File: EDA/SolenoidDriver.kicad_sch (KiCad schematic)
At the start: 16 parts, among them U9 LMR62014XMF

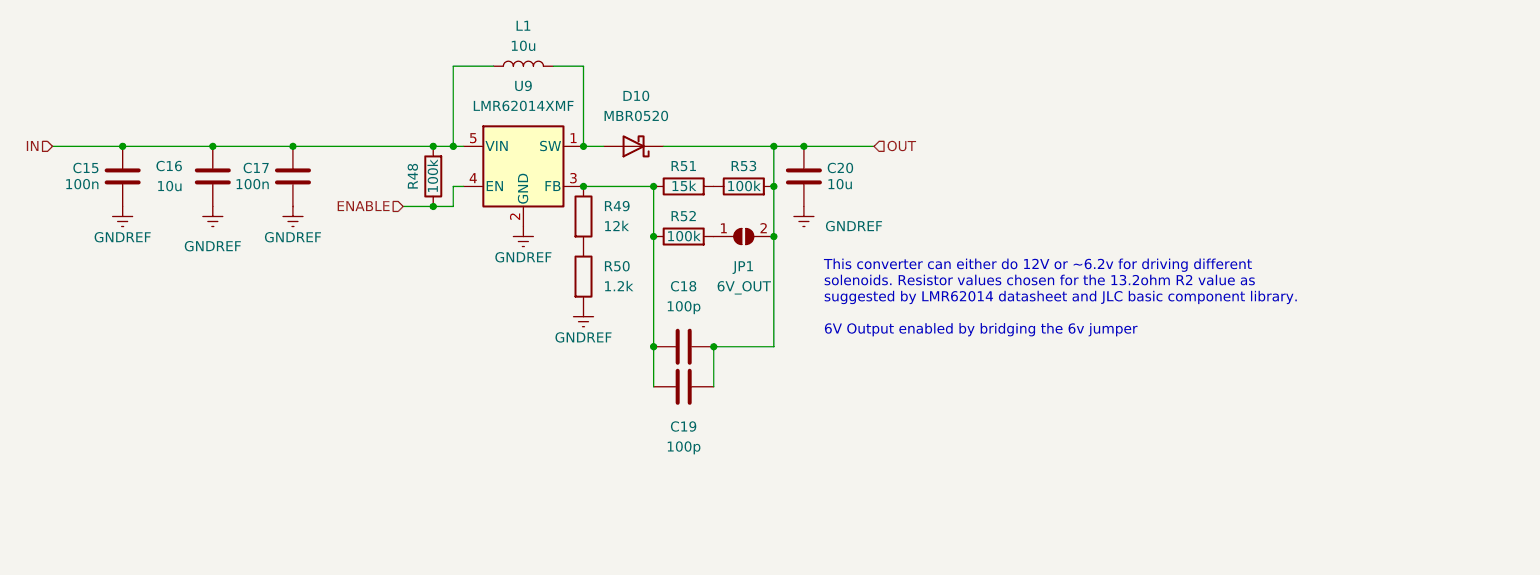
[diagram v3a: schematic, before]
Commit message: Move power logic into power distribution sheet
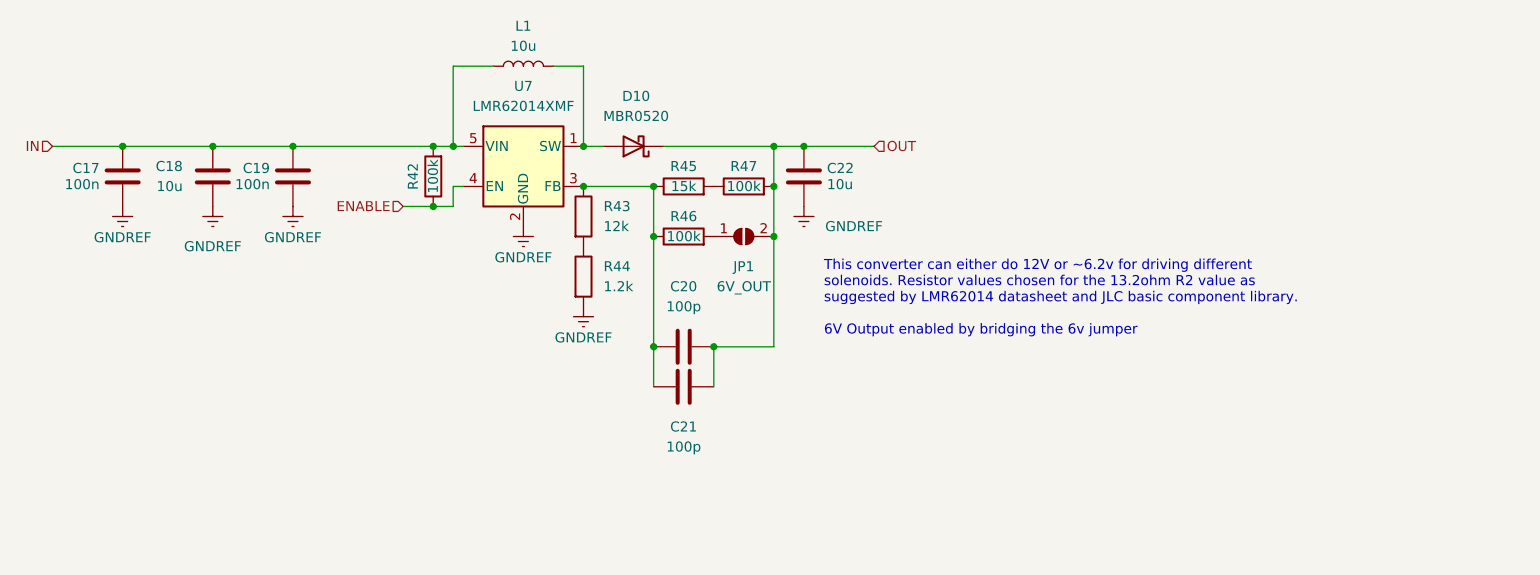
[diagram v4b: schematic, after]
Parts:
- renumbered C15 to C17, C16 to C18, C17 to C19, C18 to C20, C19 to C21, C20 to C22, R48 to R42, R49 to R43, R50 to R44, R51 to R45, R52 to R46, R53 to R47, U9 to U7
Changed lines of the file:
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@@
   (symbol (lib_id "power:GNDREF") (at 92.71 74.93 0) (unit 1)
     (in_bom yes) (on_board yes) (dnp no) (fields_autoplaced)
-    (property "Reference" "#PWR060" (at 92.71 81.28 0)
+    (property "Reference" "#PWR056" (at 92.71 81.28 0)
       (effects (font (size 1.27 1.27)) hide)
     )
@@
       (project "DiveCAN Head2"
         (path "/ab021047-3849-453b-b3dc-d234ace3779d/9021e904-ec93-4c28-9903-7bba14359351"
-          (reference "#PWR060") (unit 1)
+          (reference "#PWR056") (unit 1)
         )
       )
@@
   (symbol (lib_id "Library:R") (at 163.83 72.39 90) (unit 1)
     (in_bom yes) (on_board yes) (dnp no)
-    (property "Reference" "R51" (at 163.83 69.85 90)
+    (property "Reference" "R45" (at 163.83 69.85 90)
       (effects (font (size 1.27 1.27)))
     )
@@
       (project "DiveCAN Head2"
         (path "/ab021047-3849-453b-b3dc-d234ace3779d/9021e904-ec93-4c28-9903-7bba14359351"
-          (reference "R51") (unit 1)
+          (reference "R45") (unit 1)
         )
       )
@@
   (symbol (lib_id "Library:R") (at 151.13 76.2 0) (unit 1)
     (in_bom yes) (on_board yes) (dnp no) (fields_autoplaced)
-    (property "Reference" "R49" (at 153.67 74.93 0)
+    (property "Reference" "R43" (at 153.67 74.93 0)
       (effects (font (size 1.27 1.27)) (justify left))
     )
@@
       (project "DiveCAN Head2"
         (path "/ab021047-3849-453b-b3dc-d234ace3779d/9021e904-ec93-4c28-9903-7bba14359351"
-          (reference "R49") (unit 1)
+          (reference "R43") (unit 1)
         )
       )
@@
   (symbol (lib_id "Library:R") (at 132.08 71.12 180) (unit 1)
     (in_bom yes) (on_board yes) (dnp no)
-    (property "Reference" "R48" (at 129.54 71.12 90)
+    (property "Reference" "R42" (at 129.54 71.12 90)
       (effects (font (size 1.27 1.27)))
     )
@@
       (project "DiveCAN Head2"
         (path "/ab021047-3849-453b-b3dc-d234ace3779d/9021e904-ec93-4c28-9903-7bba14359351"
-          (reference "R48") (unit 1)
+          (reference "R42") (unit 1)
         )
       )
@@
   (symbol (lib_id "power:GNDREF") (at 151.13 87.63 0) (unit 1)
     (in_bom yes) (on_board yes) (dnp no) (fields_autoplaced)
-    (property "Reference" "#PWR064" (at 151.13 93.98 0)
+    (property "Reference" "#PWR060" (at 151.13 93.98 0)
       (effects (font (size 1.27 1.27)) hide)
     )
@@
       (project "DiveCAN Head2"
         (path "/ab021047-3849-453b-b3dc-d234ace3779d/9021e904-ec93-4c28-9903-7bba14359351"
-          (reference "#PWR064") (unit 1)
+          (reference "#PWR060") (unit 1)
         )
       )
@@
   (symbol (lib_id "Regulator_Switching:LMR62014XMF") (at 143.51 69.85 0) (unit 1)
     (in_bom yes) (on_board yes) (dnp no) (fields_autoplaced)
-    (property "Reference" "U9" (at 143.51 59.69 0)
+    (property "Reference" "U7" (at 143.51 59.69 0)
       (effects (font (size 1.27 1.27)))
     )
@@
       (project "DiveCAN Head2"
         (path "/ab021047-3849-453b-b3dc-d234ace3779d/9021e904-ec93-4c28-9903-7bba14359351"
-          (reference "U9") (unit 1)
+          (reference "U7") (unit 1)
         )
       )
@@
   (symbol (lib_id "Library:C") (at 114.3 71.12 180) (unit 1)
     (in_bom yes) (on_board yes) (dnp no) (fields_autoplaced)
-    (property "Reference" "C17" (at 111.3791 70.096 0)
+    (property "Reference" "C19" (at 111.3791 70.096 0)
       (effects (font (size 1.27 1.27)) (justify left))
     )
@@
       (project "DiveCAN Head2"
         (path "/ab021047-3849-453b-b3dc-d234ace3779d/9021e904-ec93-4c28-9903-7bba14359351"
-          (reference "C17") (unit 1)
+          (reference "C19") (unit 1)
         )
       )
@@
   (symbol (lib_id "power:GNDREF") (at 114.3 74.93 0) (unit 1)
     (in_bom yes) (on_board yes) (dnp no) (fields_autoplaced)
-    (property "Reference" "#PWR062" (at 114.3 81.28 0)
+    (property "Reference" "#PWR058" (at 114.3 81.28 0)
       (effects (font (size 1.27 1.27)) hide)
     )
@@
       (project "DiveCAN Head2"
         (path "/ab021047-3849-453b-b3dc-d234ace3779d/9021e904-ec93-4c28-9903-7bba14359351"
-          (reference "#PWR062") (unit 1)
+          (reference "#PWR058") (unit 1)
         )
       )
@@
   (symbol (lib_id "Library:R") (at 163.83 78.74 90) (unit 1)
     (in_bom yes) (on_board yes) (dnp no)
-    (property "Reference" "R52" (at 163.83 76.2 90)
+    (property "Reference" "R46" (at 163.83 76.2 90)
       (effects (font (size 1.27 1.27)))
     )
@@
       (project "DiveCAN Head2"
         (path "/ab021047-3849-453b-b3dc-d234ace3779d/9021e904-ec93-4c28-9903-7bba14359351"
-          (reference "R52") (unit 1)
+          (reference "R46") (unit 1)
         )
       )
@@
   (symbol (lib_id "Library:C") (at 104.14 71.12 0) (unit 1)
     (in_bom yes) (on_board yes) (dnp no) (fields_autoplaced)
-    (property "Reference" "C16" (at 100.33 69.85 0)
+    (property "Reference" "C18" (at 100.33 69.85 0)
       (effects (font (size 1.27 1.27)) (justify right))
     )
@@
       (project "DiveCAN Head2"
         (path "/ab021047-3849-453b-b3dc-d234ace3779d/9021e904-ec93-4c28-9903-7bba14359351"
-          (reference "C16") (unit 1)
+          (reference "C18") (unit 1)
         )
       )
@@
   (symbol (lib_id "power:GNDREF") (at 179.07 74.93 0) (unit 1)
     (in_bom yes) (on_board yes) (dnp no)
-    (property "Reference" "#PWR065" (at 179.07 81.28 0)
+    (property "Reference" "#PWR061" (at 179.07 81.28 0)
       (effects (font (size 1.27 1.27)) hide)
     )
@@
       (project "DiveCAN Head2"
         (path "/ab021047-3849-453b-b3dc-d234ace3779d/9021e904-ec93-4c28-9903-7bba14359351"
-          (reference "#PWR065") (unit 1)
+          (reference "#PWR061") (unit 1)
         )
       )
@@
   (symbol (lib_id "Library:C") (at 163.83 97.79 270) (unit 1)
     (in_bom yes) (on_board yes) (dnp no) (fields_autoplaced)
-    (property "Reference" "C19" (at 163.83 102.87 90)
+    (property "Reference" "C21" (at 163.83 102.87 90)
       (effects (font (size 1.27 1.27)))
     )
@@
       (project "DiveCAN Head2"
         (path "/ab021047-3849-453b-b3dc-d234ace3779d/9021e904-ec93-4c28-9903-7bba14359351"
-          (reference "C19") (unit 1)
+          (reference "C21") (unit 1)
         )
       )
@@
   (symbol (lib_id "Library:C") (at 163.83 92.71 270) (unit 1)
     (in_bom yes) (on_board yes) (dnp no) (fields_autoplaced)
-    (property "Reference" "C18" (at 163.83 85.09 90)
+    (property "Reference" "C20" (at 163.83 85.09 90)
       (effects (font (size 1.27 1.27)))
     )
@@
       (project "DiveCAN Head2"
         (path "/ab021047-3849-453b-b3dc-d234ace3779d/9021e904-ec93-4c28-9903-7bba14359351"
-          (reference "C18") (unit 1)
+          (reference "C20") (unit 1)
         )
       )
@@
   (symbol (lib_id "power:GNDREF") (at 143.51 77.47 0) (unit 1)
     (in_bom yes) (on_board yes) (dnp no) (fields_autoplaced)
-    (property "Reference" "#PWR063" (at 143.51 83.82 0)
+    (property "Reference" "#PWR059" (at 143.51 83.82 0)
       (effects (font (size 1.27 1.27)) hide)
     )
@@
       (project "DiveCAN Head2"
         (path "/ab021047-3849-453b-b3dc-d234ace3779d/9021e904-ec93-4c28-9903-7bba14359351"
-          (reference "#PWR063") (unit 1)
+          (reference "#PWR059") (unit 1)
         )
       )
@@
   (symbol (lib_id "Library:R") (at 151.13 83.82 0) (unit 1)
     (in_bom yes) (on_board yes) (dnp no) (fields_autoplaced)
-    (property "Reference" "R50" (at 153.67 82.55 0)
+    (property "Reference" "R44" (at 153.67 82.55 0)
       (effects (font (size 1.27 1.27)) (justify left))
     )
@@
       (project "DiveCAN Head2"
         (path "/ab021047-3849-453b-b3dc-d234ace3779d/9021e904-ec93-4c28-9903-7bba14359351"
-          (reference "R50") (unit 1)
+          (reference "R44") (unit 1)
         )
       )
@@
   (symbol (lib_id "Library:R") (at 171.45 72.39 90) (unit 1)
     (in_bom yes) (on_board yes) (dnp no)
-    (property "Reference" "R53" (at 171.45 69.85 90)
+    (property "Reference" "R47" (at 171.45 69.85 90)
       (effects (font (size 1.27 1.27)))
     )
@@
       (project "DiveCAN Head2"
         (path "/ab021047-3849-453b-b3dc-d234ace3779d/9021e904-ec93-4c28-9903-7bba14359351"
-          (reference "R53") (unit 1)
+          (reference "R47") (unit 1)
         )
       )
@@
   (symbol (lib_id "Library:C") (at 179.07 71.12 0) (unit 1)
     (in_bom yes) (on_board yes) (dnp no) (fields_autoplaced)
-    (property "Reference" "C20" (at 181.991 70.096 0)
+    (property "Reference" "C22" (at 181.991 70.096 0)
       (effects (font (size 1.27 1.27)) (justify left))
     )
@@
       (project "DiveCAN Head2"
         (path "/ab021047-3849-453b-b3dc-d234ace3779d/9021e904-ec93-4c28-9903-7bba14359351"
-          (reference "C20") (unit 1)
+          (reference "C22") (unit 1)
         )
       )
@@
   (symbol (lib_id "power:GNDREF") (at 104.14 74.93 0) (unit 1)
     (in_bom yes) (on_board yes) (dnp no) (fields_autoplaced)
-    (property "Reference" "#PWR061" (at 104.14 81.28 0)
+    (property "Reference" "#PWR057" (at 104.14 81.28 0)
       (effects (font (size 1.27 1.27)) hide)
     )
@@
       (project "DiveCAN Head2"
         (path "/ab021047-3849-453b-b3dc-d234ace3779d/9021e904-ec93-4c28-9903-7bba14359351"
-          (reference "#PWR061") (unit 1)
+          (reference "#PWR057") (unit 1)
         )
       )
@@
   (symbol (lib_id "Library:C") (at 92.71 71.12 180) (unit 1)
     (in_bom yes) (on_board yes) (dnp no) (fields_autoplaced)
-    (property "Reference" "C15" (at 89.7891 70.096 0)
+    (property "Reference" "C17" (at 89.7891 70.096 0)
       (effects (font (size 1.27 1.27)) (justify left))
     )
@@
       (project "DiveCAN Head2"
         (path "/ab021047-3849-453b-b3dc-d234ace3779d/9021e904-ec93-4c28-9903-7bba14359351"
-          (reference "C15") (unit 1)
-        )
-      )
+          (reference "C17") (unit 1)
+        )
+      )

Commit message: Add input protection to the power distribution
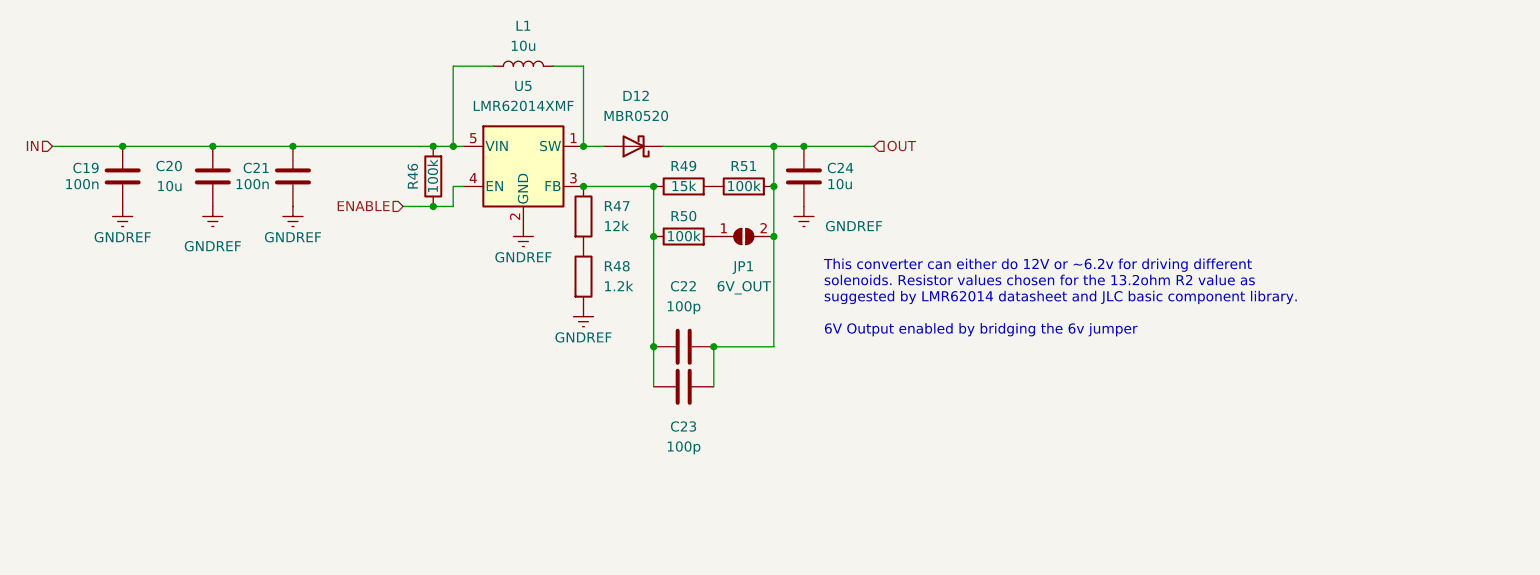
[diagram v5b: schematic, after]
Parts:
- JP1: footprint (none) -> Jumper:SolderJumper-2_P1.3mm_Open_TrianglePad1.0x1.5mm
- renumbered C17 to C19, C18 to C20, C19 to C21, C20 to C22, C21 to C23, C22 to C24, D10 to D12, R42 to R46, R43 to R47, R44 to R48, R45 to R49, R46 to R50, R47 to R51, U7 to U5

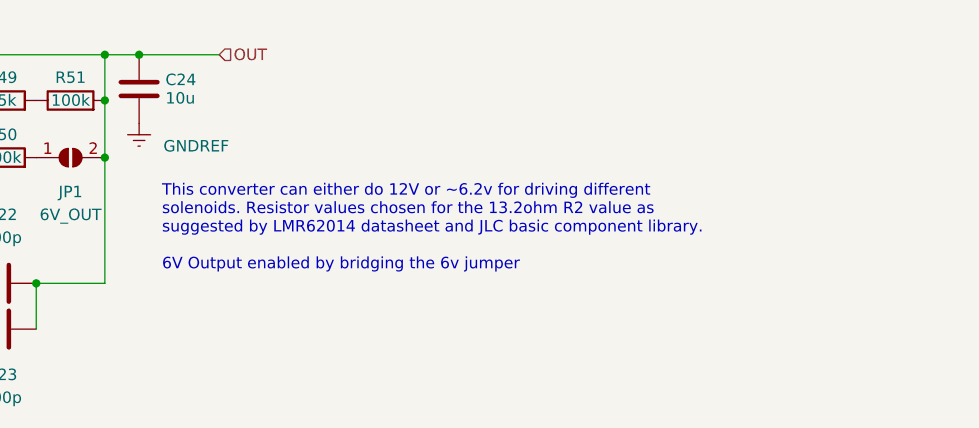
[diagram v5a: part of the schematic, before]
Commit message: Change solenoid power switch to TPS2121
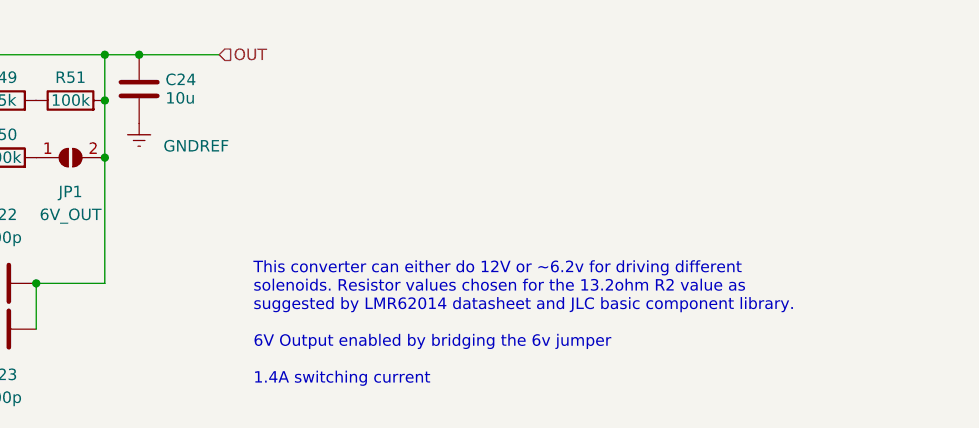
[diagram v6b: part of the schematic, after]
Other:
- note added: "This converter can either do 12V or ~6.2v for driving different solenoids. Resistor values chosen for the 13.2ohm R2 value as suggested by LMR62014 datasheet and JLC basic component library. 6V Output enabled by bridging the 6v jumper 1.4A switching current"
- note removed: "This converter can either do 12V or ~6.2v for driving different solenoids. Resistor values chosen for the 13.2ohm R2 value as suggested by LMR62014 datasheet and JLC basic component library. 6V Output enabled by bridging the 6v jumper"
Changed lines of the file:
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@@
     (stroke (width 0) (type default))
   )
-  (text "This converter can either do 12V or ~6.2v for driving different\nsolenoids. Resistor values chosen for the 13.2ohm R2 value as \nsuggested by LMR62014 datasheet and JLC basic component library.\n\n6V Output enabled by bridging the 6v jumper"
-    (at 181.61 91.44 0)
+  (text "This converter can either do 12V or ~6.2v for driving different\nsolenoids. Resistor values chosen for the 13.2ohm R2 value as \nsuggested by LMR62014 datasheet and JLC basic component library.\n\n6V Output enabled by bridging the 6v jumper\n\n1.4A switching current"
+    (at 191.77 104.14 0)
     (effects (font (size 1.27 1.27)) (justify left bottom))
   )

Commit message: Draft Rev2 PCB
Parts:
- L1: footprint (none) -> Library:L_SunItech_SLO0530H; MPN C879423 -> C325966
- U5: MPN (none) -> C468235
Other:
- note added: "This converter can either do 12V or ~6.2v for driving different solenoids. Resistor values chosen for the 13.2kohm R2 value as suggested by LMR62014 datasheet and JLC basic component library. 6V Output enabled by bridging the 6v jumper 1.4A switching current"
- note removed: "This converter can either do 12V or ~6.2v for driving different solenoids. Resistor values chosen for the 13.2ohm R2 value as suggested by LMR62014 datasheet and JLC basic component library. 6V Output enabled by bridging the 6v jumper 1.4A switching current"
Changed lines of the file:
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@@
     (stroke (width 0) (type default))
   )
-  (text "This converter can either do 12V or ~6.2v for driving different\nsolenoids. Resistor values chosen for the 13.2ohm R2 value as \nsuggested by LMR62014 datasheet and JLC basic component library.\n\n6V Output enabled by bridging the 6v jumper\n\n1.4A switching current"
-    (at 191.77 104.14 0)
+  (text "This converter can either do 12V or ~6.2v for driving different\nsolenoids. Resistor values chosen for the 13.2kohm R2 value as \nsuggested by LMR62014 datasheet and JLC basic component library.\n\n6V Output enabled by bridging the 6v jumper\n\n1.4A switching current"
+    (at 184.15 95.25 0)
     (effects (font (size 1.27 1.27)) (justify left bottom))
   )
@@
       (effects (font (size 1.27 1.27)) hide)
     )
+    (property "MPN" "C468235" (at 143.51 69.85 0)
+      (effects (font (size 1.27 1.27)) hide)
+    )
     (pin "1")
     (pin "2")
@@
       (effects (font (size 1.27 1.27)))
     )
-    (property "Footprint" "" (at 143.51 57.15 0)
-      (effects (font (size 1.27 1.27)) hide)
-    )
-    (property "Datasheet" "https://au.mouser.com/datasheet/2/390/125CDMCCDS__en_-1375057.pdf" (at 143.51 57.15 0)
-      (effects (font (size 1.27 1.27)) hide)
-    )
-    (property "MPN" "C879423" (at 143.51 57.15 0)
-      (effects (font (size 1.27 1.27)) hide)
-    )
+    (property "Footprint" "Library:L_SunItech_SLO0530H" (at 143.51 57.15 0)
+      (effects (font (size 1.27 1.27)) hide)
+    )
+    (property "Datasheet" "" (at 143.51 57.15 0)
+      (effects (font (size 1.27 1.27)) hide)
+    )
+    (property "MPN" "   C325966" (at 143.51 57.15 0)
+      (effects (font (size 1.27 1.27)) hide)
+    )
